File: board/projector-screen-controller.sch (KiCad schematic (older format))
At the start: 9 parts, among them J2 MSTBVA-3-G, J3 MCV-3-G, J4 MCV-3-G, J5 MCV-3-G, J6 MSTBVA-6-G, J7 MCV-3-G

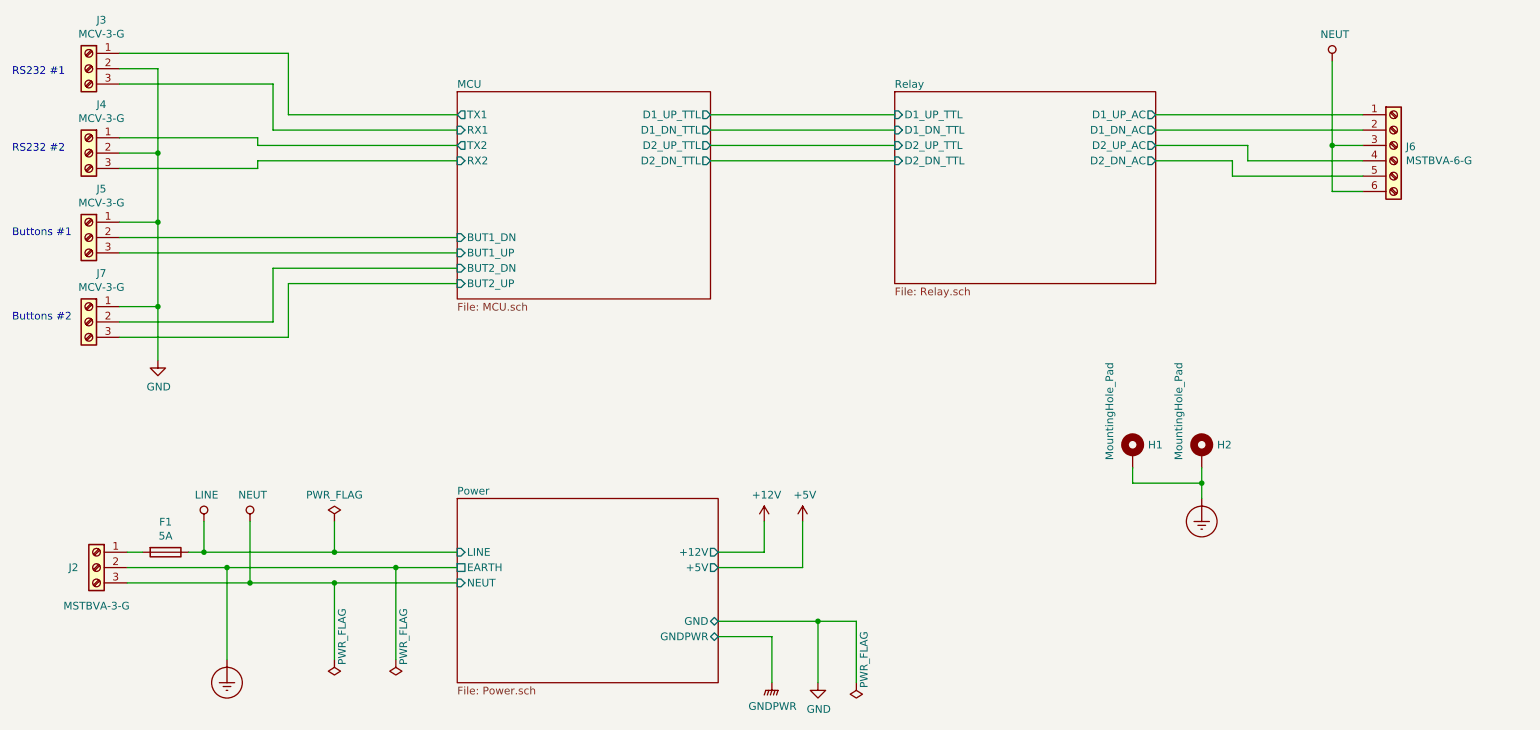
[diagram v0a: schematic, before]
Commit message: Add/correct a bunch of part numbers
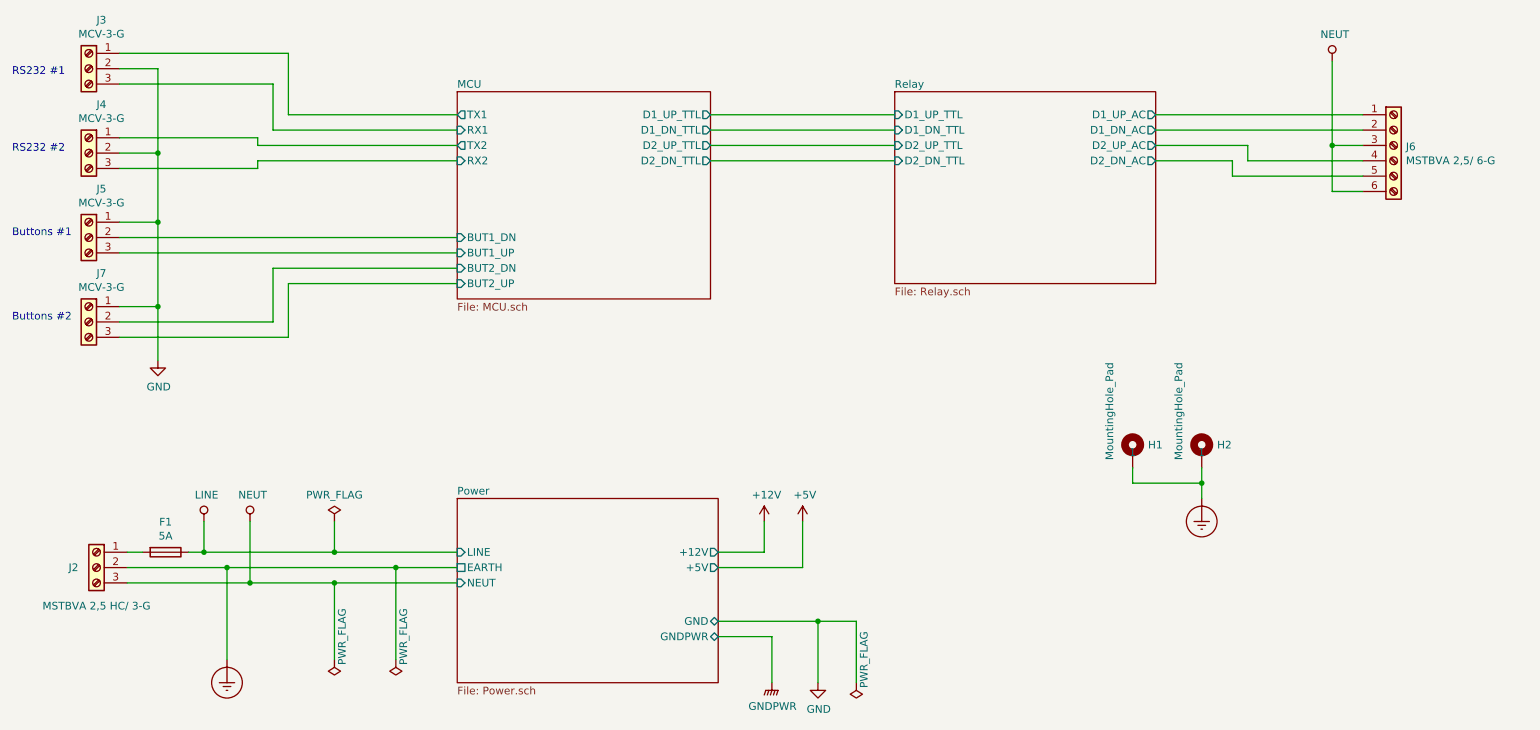
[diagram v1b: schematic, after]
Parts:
- H1, H2: DNP (none) -> 1
- J2: value MSTBVA-3-G -> MSTBVA 2,5 HC/ 3-G; Src1 (none) -> Mouser; Src1 Part (none) -> 651-1924208; Src1 URL (none) -> https://www.mouser.com/ProductDetail/651-1924208; mpn (none) -> 1924208; part# 1924208 -> (none)
- J3, J5, J7: Src1 (none) -> Mouser; Src1 Part (none) -> 651-1843619; Src1 URL (none) -> https://www.mouser.com/ProductDetail/651-1843619; mfr (none) -> Phoenix Connect; mpn (none) -> 1843619
- J4: Src1 (none) -> Mouser; Src1 Part (none) -> 651-1843619; Src1 URL (none) -> https://www.mouser.com/ProductDetail/651-1843619; mfr (none) -> Phoenx Connect; mpn (none) -> 1843619
- J6: value MSTBVA-6-G -> MSTBVA 2,5/ 6-G; Src1 (none) -> Mouser; Src1 Part (none) -> 651-1755558; Src1 URL (none) -> https://www.mouser.com/ProductDetail/651-1755558; mfr (none) -> Phoenix Connect; mpn (none) -> 1755558
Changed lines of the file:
@@
 F 2 "Connector_Phoenix_MC:PhoenixContact_MCV_1,5_3-G-3.5_1x03_P3.50mm_Vertical" H 1350 2050 50  0001 C CNN
 F 3 "~" H 1350 2050 50  0001 C CNN
+F 4 "Phoenix Connect" H 1350 2050 50  0001 C CNN "mfr"
+F 5 "1843619" H 1350 2050 50  0001 C CNN "mpn"
+F 6 "Mouser" H 1350 2050 50  0001 C CNN "Src1"
+F 7 "651-1843619" H 1350 2050 50  0001 C CNN "Src1 Part"
+F 8 "https://www.mouser.com/ProductDetail/651-1843619" H 1350 2050 50  0001 C CNN "Src1 URL"
 	1    1350 2050
 	-1   0    0    -1
@@
 F 2 "Connector_Phoenix_MC:PhoenixContact_MCV_1,5_3-G-3.5_1x03_P3.50mm_Vertical" H 1350 2600 50  0001 C CNN
 F 3 "~" H 1350 2600 50  0001 C CNN
+F 4 "Phoenx Connect" H 1350 2600 50  0001 C CNN "mfr"
+F 5 "1843619" H 1350 2600 50  0001 C CNN "mpn"
+F 6 "Mouser" H 1350 2600 50  0001 C CNN "Src1"
+F 7 "651-1843619" H 1350 2600 50  0001 C CNN "Src1 Part"
+F 8 "https://www.mouser.com/ProductDetail/651-1843619" H 1350 2600 50  0001 C CNN "Src1 URL"
 	1    1350 2600
 	-1   0    0    -1
@@
 F 2 "Connector_Phoenix_MC:PhoenixContact_MCV_1,5_3-G-3.5_1x03_P3.50mm_Vertical" H 1350 3150 50  0001 C CNN
 F 3 "~" H 1350 3150 50  0001 C CNN
+F 4 "Phoenix Connect" H 1350 3150 50  0001 C CNN "mfr"
+F 5 "1843619" H 1350 3150 50  0001 C CNN "mpn"
+F 6 "Mouser" H 1350 3150 50  0001 C CNN "Src1"
+F 7 "651-1843619" H 1350 3150 50  0001 C CNN "Src1 Part"
+F 8 "https://www.mouser.com/ProductDetail/651-1843619" H 1350 3150 50  0001 C CNN "Src1 URL"
 	1    1350 3150
 	-1   0    0    -1
@@
 P 9850 2550
 F 0 "J6" H 9930 2542 50  0000 L CNN
-F 1 "MSTBVA-6-G" H 9930 2451 50  0000 L CNN
+F 1 "MSTBVA 2,5/ 6-G" H 9930 2451 50  0000 L CNN
 F 2 "Connector_Phoenix_MSTB:PhoenixContact_MSTBVA_2,5_6-G_1x06_P5.00mm_Vertical" H 9850 2550 50  0001 C CNN
 F 3 "~" H 9850 2550 50  0001 C CNN
+F 4 "Phoenix Connect" H 9850 2550 50  0001 C CNN "mfr"
+F 5 "1755558" H 9850 2550 50  0001 C CNN "mpn"
+F 6 "Mouser" H 9850 2550 50  0001 C CNN "Src1"
+F 7 "651-1755558" H 9850 2550 50  0001 C CNN "Src1 Part"
+F 8 "https://www.mouser.com/ProductDetail/651-1755558" H 9850 2550 50  0001 C CNN "Src1 URL"
 	1    9850 2550
 	1    0    0    -1
@@
 F 2 "Connector_Phoenix_MC:PhoenixContact_MCV_1,5_3-G-3.5_1x03_P3.50mm_Vertical" H 1350 3700 50  0001 C CNN
 F 3 "~" H 1350 3700 50  0001 C CNN
+F 4 "Phoenix Connect" H 1350 3700 50  0001 C CNN "mfr"
+F 5 "1843619" H 1350 3700 50  0001 C CNN "mpn"
+F 6 "Mouser" H 1350 3700 50  0001 C CNN "Src1"
+F 7 "651-1843619" H 1350 3700 50  0001 C CNN "Src1 Part"
+F 8 "https://www.mouser.com/ProductDetail/651-1843619" H 1350 3700 50  0001 C CNN "Src1 URL"
 	1    1350 3700
 	-1   0    0    -1
@@
 F 2 "Mounting_Holes:MountingHole_3.7mm_Pad_Via" H 8600 4550 50  0001 C CNN
 F 3 "~" H 8600 4550 50  0001 C CNN
+F 4 "1" H 8600 4550 50  0000 C CNN "DNP"
 	1    8600 4550
 	1    0    0    -1
@@
 F 2 "Mounting_Holes:MountingHole_3.7mm_Pad_Via" H 8150 4550 50  0001 C CNN
 F 3 "~" H 8150 4550 50  0001 C CNN
+F 4 "1" H 8150 4550 50  0000 C CNN "DNP"
 	1    8150 4550
 	1    0    0    -1
@@
 P 1400 5300
 F 0 "J2" H 1550 5300 50  0000 C CNN
-F 1 "MSTBVA-3-G" H 1400 5050 50  0000 C CNN
+F 1 "MSTBVA 2,5 HC/ 3-G" H 1400 5050 50  0000 C CNN
 F 2 "Connector_Phoenix_MSTB:PhoenixContact_MSTBVA_2,5_3-G_1x03_P5.00mm_Vertical" H 1400 5300 50  0001 C CNN
 F 3 "~" H 1400 5300 50  0001 C CNN
 F 4 "Phoenix Connect" H 1400 5300 50  0001 C CNN "mfr"
-F 5 "1924208" H 1400 5300 50  0001 C CNN "part#"
+F 5 "1924208" H 1400 5300 50  0001 C CNN "mpn"
+F 6 "Mouser" H 1400 5300 50  0001 C CNN "Src1"
+F 7 "651-1924208" H 1400 5300 50  0001 C CNN "Src1 Part"
+F 8 "https://www.mouser.com/ProductDetail/651-1924208" H 1400 5300 50  0001 C CNN "Src1 URL"
 	1    1400 5300
 	-1   0    0    -1

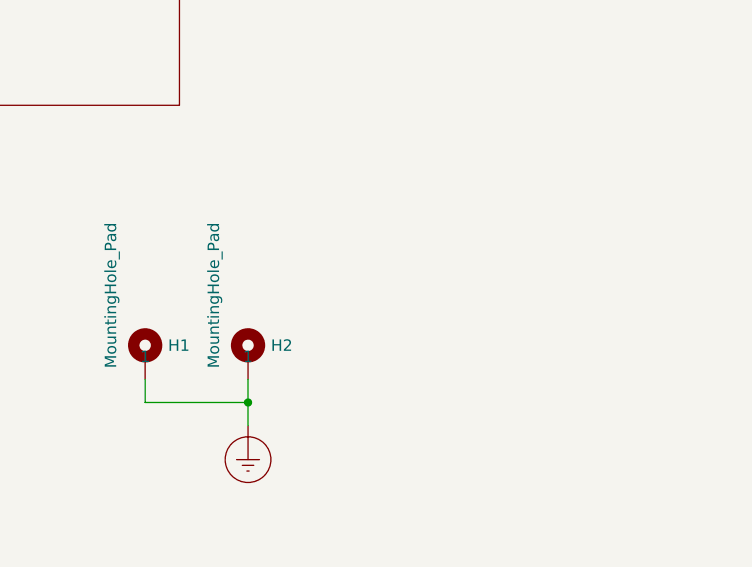
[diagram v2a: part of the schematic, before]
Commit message: Update xtal load capacitors, fix left mounting holes
* Try some 33pF caps for the crystal.
* Reflect the left side mounting holes in the schematic.
* Reroute one RS232 TTL line; though now more stuff runs under the clock
  lines so may move all the RS232 TTL traces later.
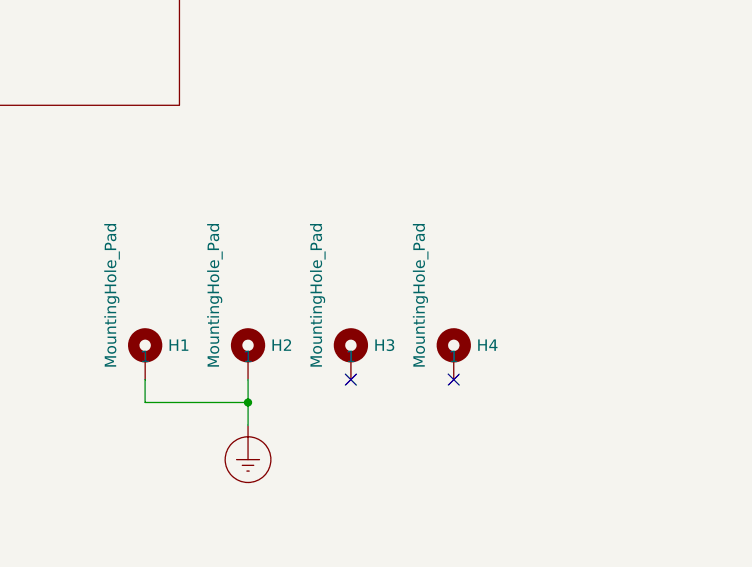
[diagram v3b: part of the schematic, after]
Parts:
- added H3, H4: MountingHole_Pad, Mounting_Holes:MountingHole_3.7mm_Pad_Via, symbol Mechanical:MountingHole_Pad
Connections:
- no-connect marks 0 -> 2
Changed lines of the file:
@@
 Sheet 1 4
 Title "Projector Screen Controller"
-Date "2019-09-21"
+Date "2019-09-22"
 Rev "0.2"
 Comp "Flirble Open Source"
@@
 	-1   0    0    -1
 $EndComp
+$Comp
+L Mechanical:MountingHole_Pad H3
+U 1 1 5D8CE4E9
+P 9050 4550
+F 0 "H3" H 9150 4599 50  0000 L CNN
+F 1 "MountingHole_Pad" V 8900 4500 50  0000 L CNN
+F 2 "Mounting_Holes:MountingHole_3.7mm_Pad_Via" H 9050 4550 50  0001 C CNN
+F 3 "~" H 9050 4550 50  0001 C CNN
+F 4 "1" H 9050 4550 50  0000 C CNN "DNP"
+	1    9050 4550
+	1    0    0    -1
+$EndComp
+$Comp
+L Mechanical:MountingHole_Pad H4
+U 1 1 5D8D01BB
+P 9500 4550
+F 0 "H4" H 9600 4599 50  0000 L CNN
+F 1 "MountingHole_Pad" V 9350 4500 50  0000 L CNN
+F 2 "Mounting_Holes:MountingHole_3.7mm_Pad_Via" H 9500 4550 50  0001 C CNN
+F 3 "~" H 9500 4550 50  0001 C CNN
+F 4 "1" H 9500 4550 50  0000 C CNN "DNP"
+	1    9500 4550
+	1    0    0    -1
+$EndComp
+NoConn ~ 9050 4650
+NoConn ~ 9500 4650
 $EndSCHEMATC
